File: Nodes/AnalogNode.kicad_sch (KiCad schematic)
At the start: 19 parts, among them T2 Conn_01x01, U11 STM32G431RBTx, Y2 SG-8018CE_8.0000M-TJHPA3

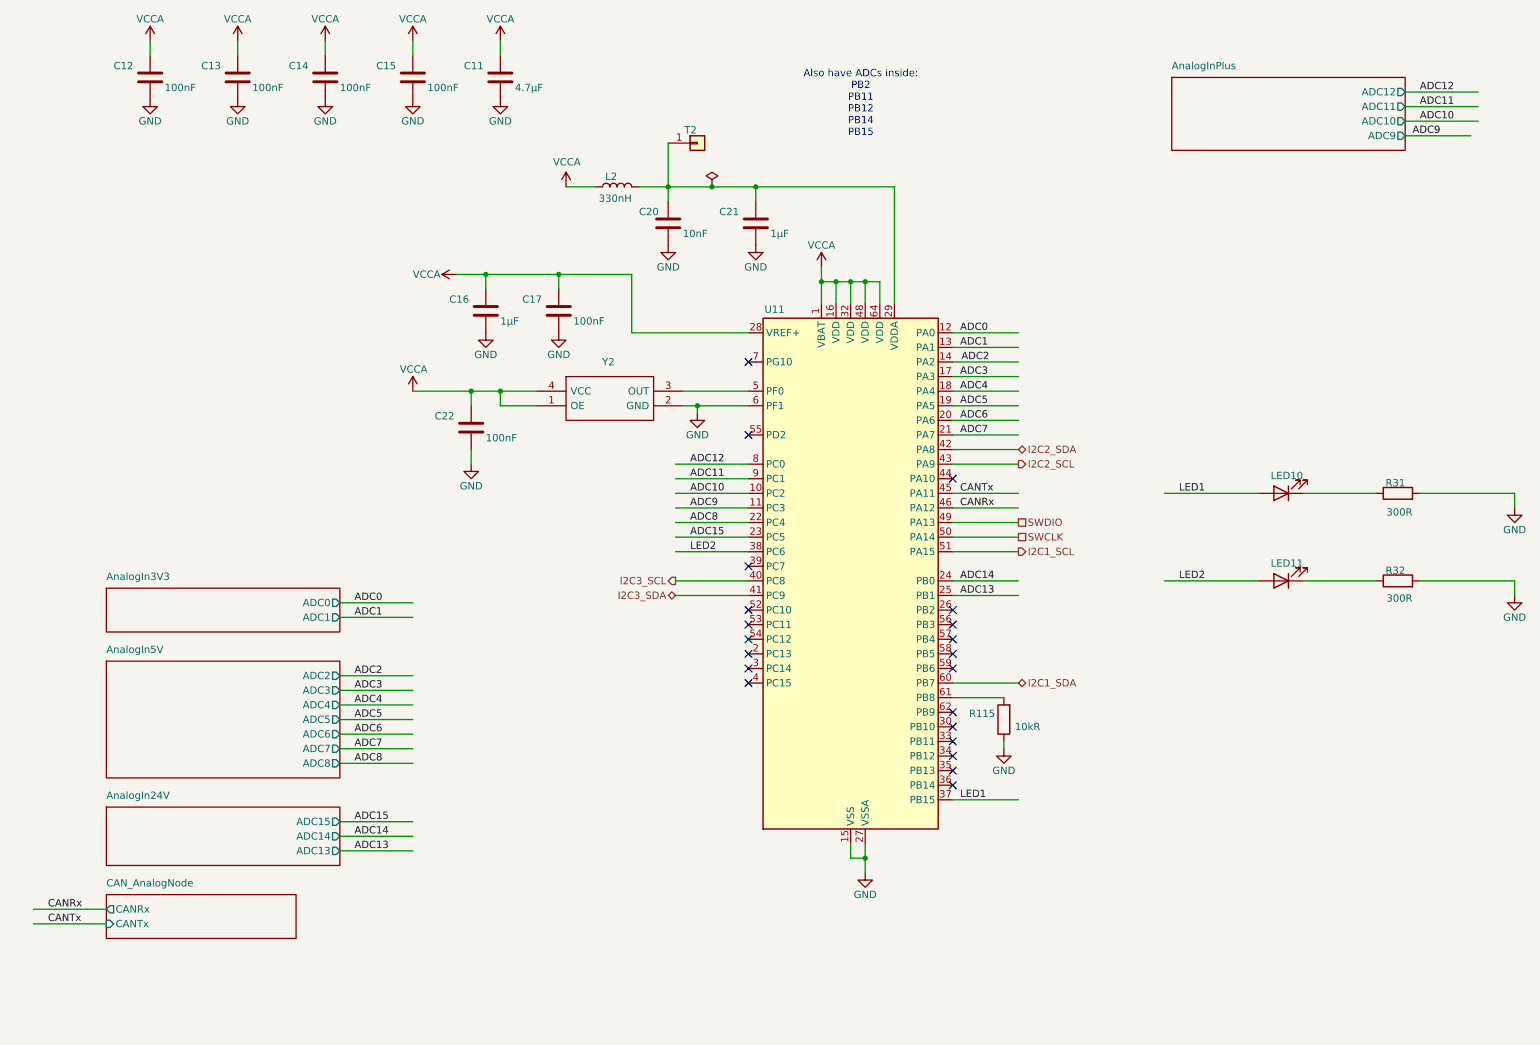
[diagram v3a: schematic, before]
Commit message: Nodes v2.2.5
- New High-Side Driver (Same footprint, just new info)
- Two resistors added for 3V3 Filters, which can be used to implement voltage divider
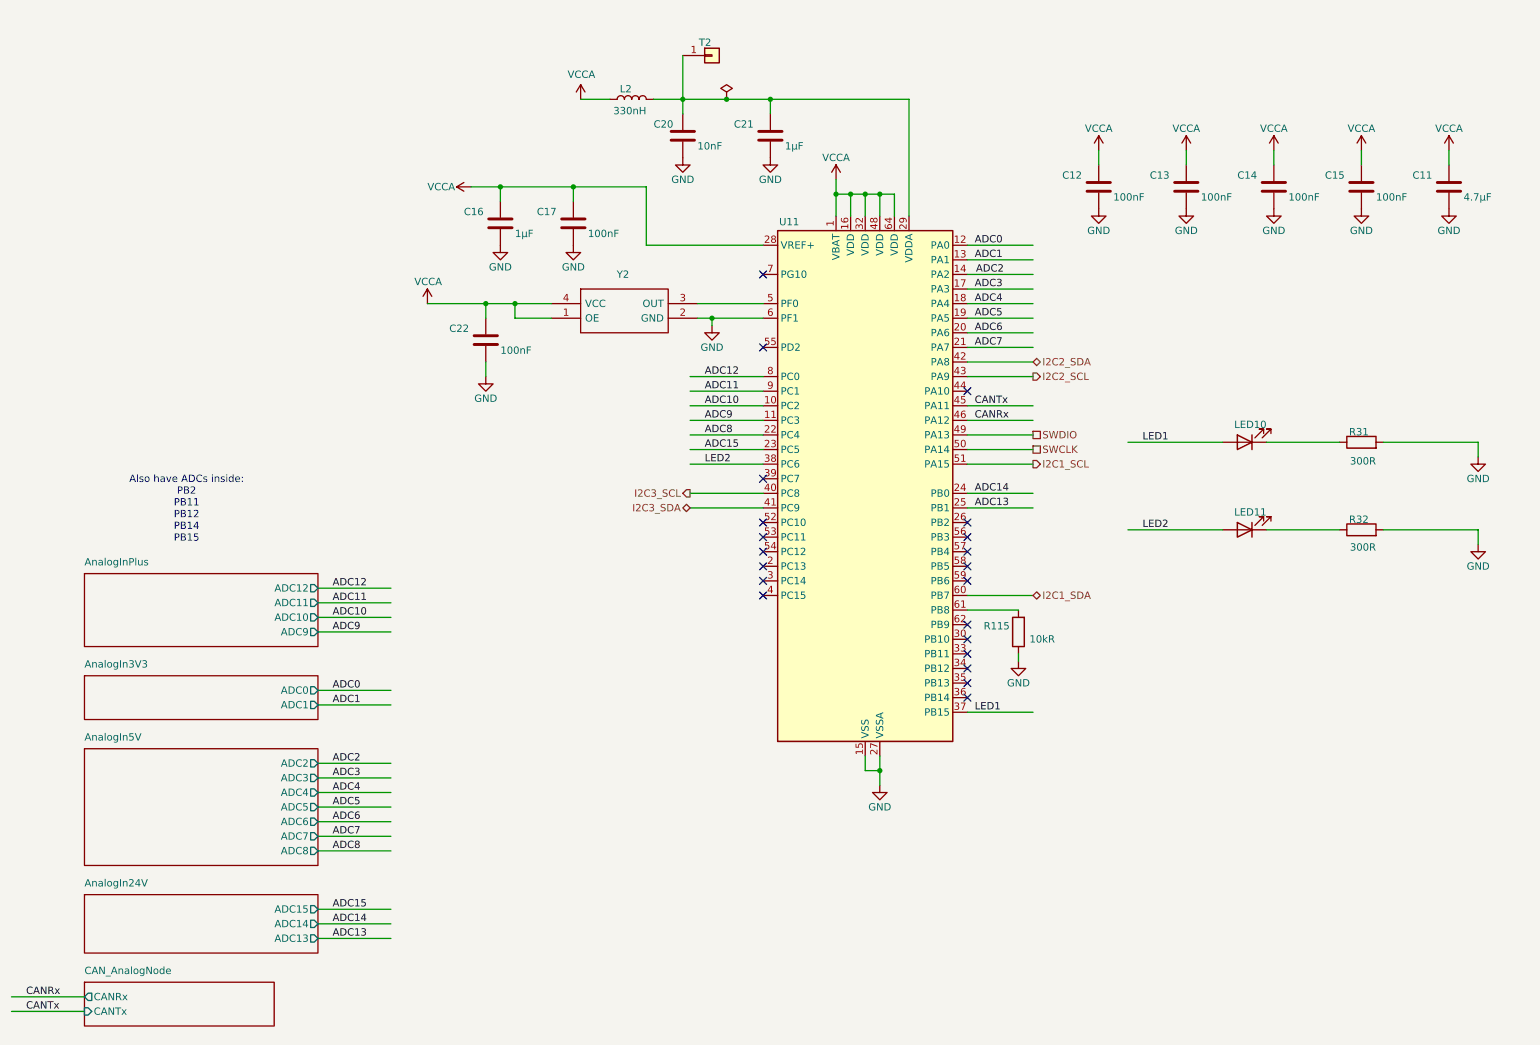
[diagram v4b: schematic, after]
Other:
- moved on the sheet: C11, C12, C13, C14, C15, C16, C17, C20, C21, C22, L2, LED10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

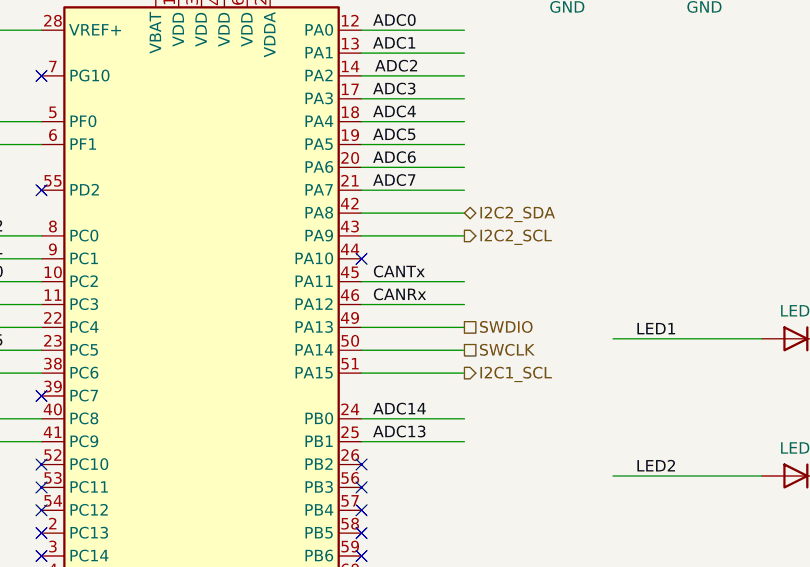
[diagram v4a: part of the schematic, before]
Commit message: Nodes v2.2.6 Revision 1.1
- CAN connection mistake for Analog Node was fixed
- Updated datasheet about CAN
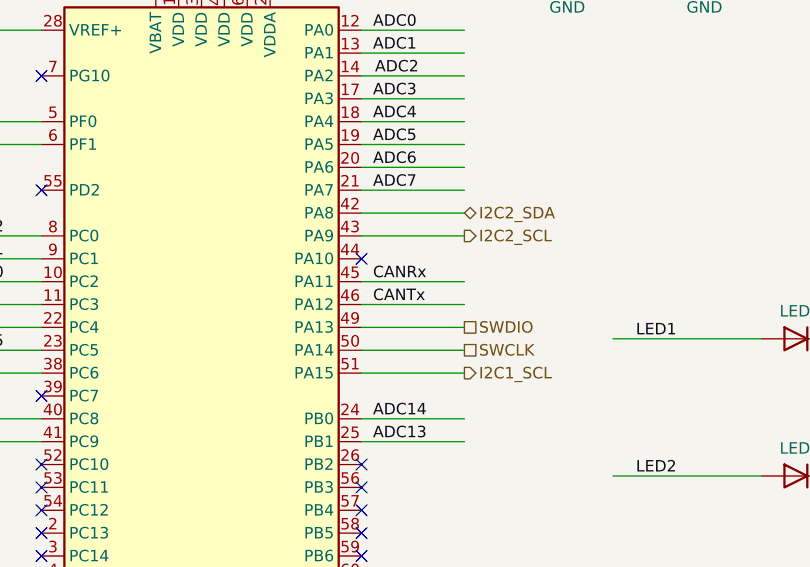
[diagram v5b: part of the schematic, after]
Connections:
- net CANRx: now also U11.45 (PA11); no longer U11.46 (PA12)
- net CANTx: now also U11.46 (PA12); no longer U11.45 (PA11)
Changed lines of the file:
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@@
+		)
+	)
+	(label "CANTx"
+		(at 186.69 87.63 0)
+		(fields_autoplaced yes)
+		(effects
+			(font
+				(size 1.27 1.27)
+			)
+			(justify left bottom)
 		)
 	)
@@
 		)
 	)
-	(label "CANTx"
-		(at 186.69 85.09 0)
-		(fields_autoplaced yes)
-		(effects
-			(font
-				(size 1.27 1.27)
-			)
-			(justify left bottom)
-		)
-	)
 	(label "ADC12"
 		(at 139.7 80.01 0)
@@
 		)
 	)
-	(label "CANRx"
-		(at 186.69 87.63 0)
-		(fields_autoplaced yes)
-		(effects
-			(font
-				(size 1.27 1.27)
-			)
-			(justify left bottom)
-		)
-	)
 	(label "ADC11"
 		(at 74.93 119.38 0)
 		(fields_autoplaced yes)
 		(effects
+			(font
+				(size 1.27 1.27)
+			)
+			(justify left bottom)
+		)
+	)
+	(label "CANRx"
+		(at 186.69 85.09 0)
+		(fields_autoplaced yes)
+		(effects
